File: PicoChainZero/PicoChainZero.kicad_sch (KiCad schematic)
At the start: 16 parts, among them J1 RJ45, J2 RJ45, J4 Screw Terminal, J5 Conn_02x20_Odd_Even, J6 Screw Terminal, J7 USB_C_Receptacle_USB2.0_14P, U1 LM78M05_TO252, U2 PCA9615DP, U3 FT232RL

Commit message: Added licences and PDF schematics
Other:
- title: (none) -> PicoChain Zero Reference Device Implementation
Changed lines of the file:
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@@
 	(generator_version "8.0")
 	(paper "A4")
+	(title_block
+		(title "PicoChain Zero Reference Device Implementation")
+		(date "2024-08-22")
+		(rev "v1.1")
+		(comment 2 "http://www.tapr.org/OHL")
+		(comment 3 "Licence: The TAPR Open Hardware License")
+		(comment 4 "Author: Jason Alexander")
+	)
 	(junction
 		(at 180.34 100.33)

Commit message: Regenerated gerbers
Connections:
- net +5V: now also U3.4 (VCCIO)
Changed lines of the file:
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@@
+	(wire
+		(pts
+			(xy 107.95 53.34) (xy 107.95 57.15)
+		)
+		(stroke
+			(width 0)
+			(type default)
+		)
+	)
 	(wire
 		(pts
@@
 					(unit 1)
 				)
+			)
+		)
+	)
+	(symbol
+		(lib_id "power:+5V")
+		(at 107.95 53.34 0)
+		(unit 1)
+		(exclude_from_sim no)
+		(in_bom yes)
+		(on_board yes)
+		(dnp no)
+		(property "Reference" "#PWR024"
+			(at 107.95 57.15 0)
+			(effects
+				(font
+					(size 1.27 1.27)
+				)
+				(hide yes)
+			)
+		)
+		(property "Value" "+5V"
+			(at 105.918 49.53 0)
+			(effects
+				(font
+					(size 1.27 1.27)
+				)
+				(justify left)
+			)
+		)
+		(property "Footprint" ""
+			(at 107.95 53.34 0)
+			(effects
+				(font
+					(size 1.27 1.27)
+				)
+				(hide yes)
+			)
+		)
+		(property "Datasheet" ""
+			(at 107.95 53.34 0)
+			(effects
+				(font
+					(size 1.27 1.27)
+				)
+				(hide yes)
+			)
+		)
+		(property "Description" "Power symbol creates a global label with name \"+5V\""
+			(at 107.95 53.34 0)
+			(effects
+				(font
+					(size 1.27 1.27)
+				)
+				(hide yes)
+			)
+		)
+		(pin "1"
+		)
+		(instances
+			(project "PicoChainZero"
+				(path "/bf05c66b-7ba7-46d1-8dac-29939cd00b00"
+					(reference "#PWR024")
+					(unit 1)
+				)

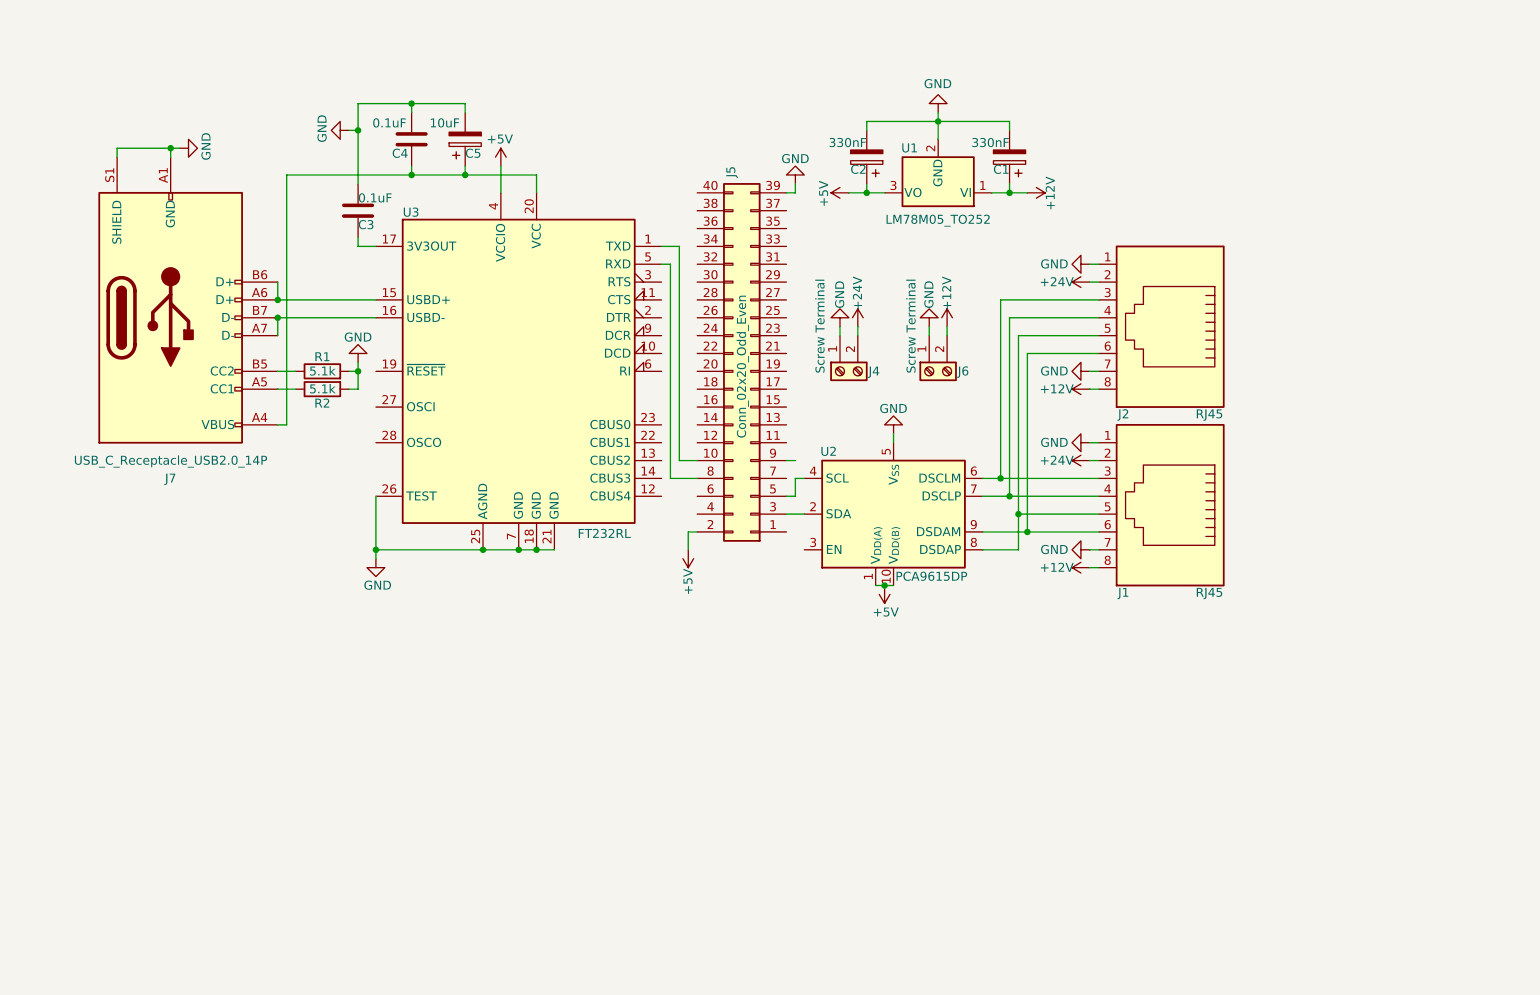
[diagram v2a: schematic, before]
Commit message: Updated PicoChainZero base board.
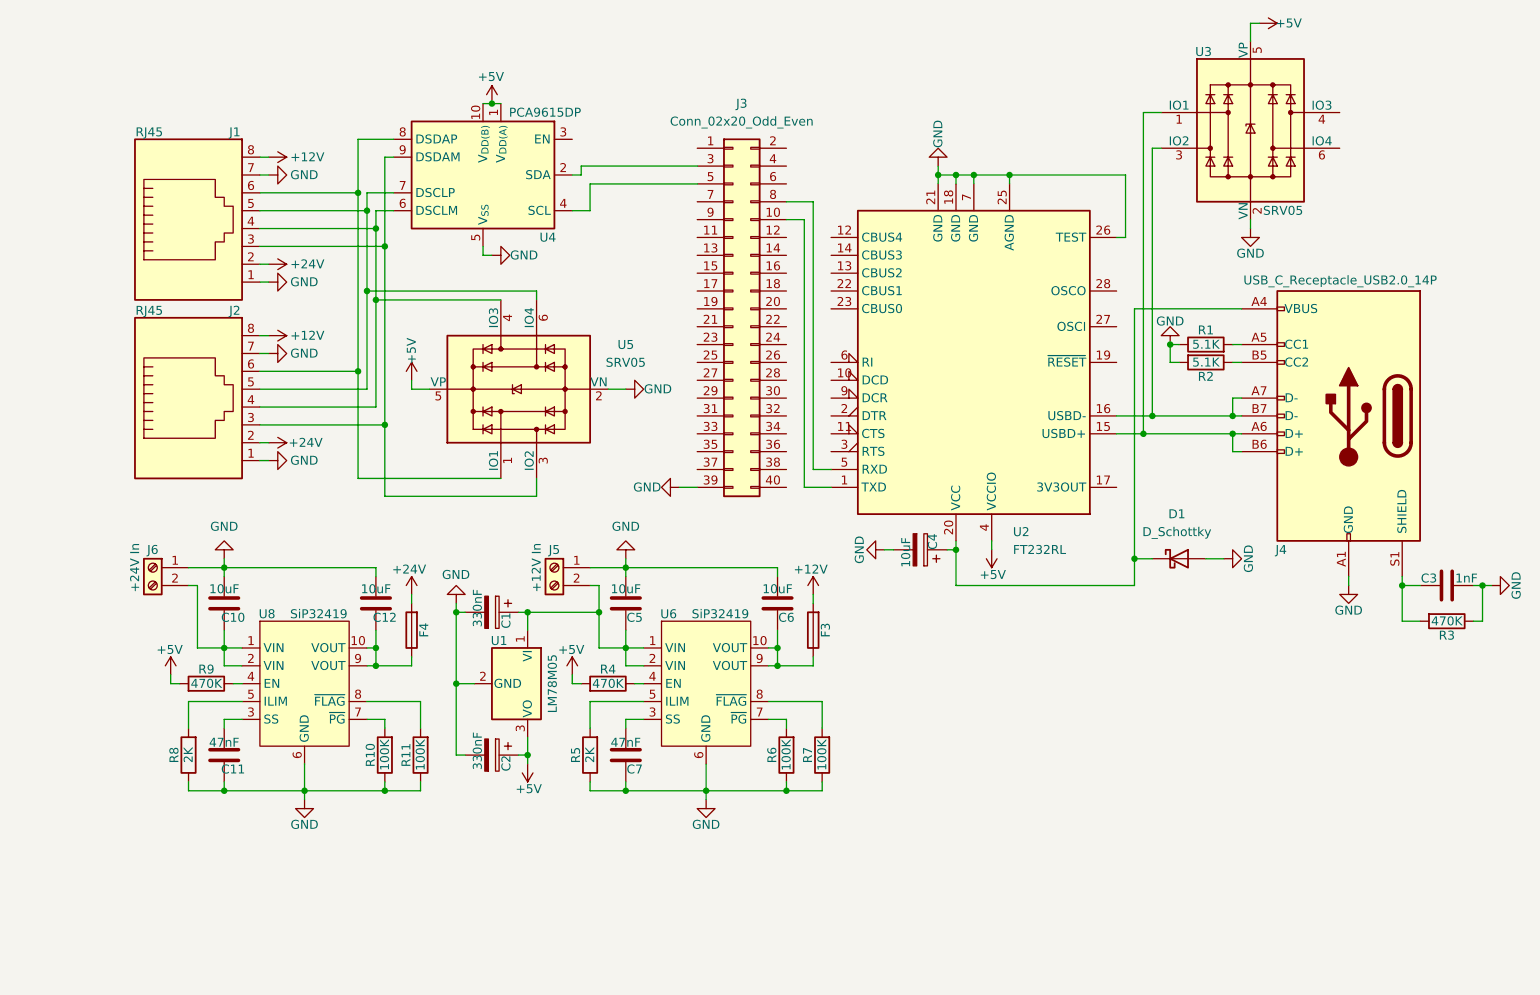
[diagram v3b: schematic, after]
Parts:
- removed C4: 0.1uF, Capacitor_SMD:C_0805_2012Metric, symbol Device:C
- removed C5: 10uF, Capacitor_Tantalum_SMD:CP_EIA-3216-18_Kemet-A, symbol Device:C_Polarized
- removed J4: Screw Terminal, TerminalBlock_Phoenix:TerminalBlock_Phoenix_MKDS-1,5-2-5.08_1x02_P5.08mm_Horizontal, symbol Connector:Screw_Terminal_01x02
- removed J5: Conn_02x20_Odd_Even, Connector_PinHeader_2.54mm:PinHeader_2x20_P2.54mm_Vertical, symbol Connector_Generic:Conn_02x20_Odd_Even
- removed J7: USB_C_Receptacle_USB2.0_14P, Connector_USB:USB_C_Receptacle_GCT_USB4085, symbol Connector:USB_C_Receptacle_USB2.0_14P
- removed U3: FT232RL, Package_SO:SSOP-28_5.3x10.2mm_P0.65mm, symbol Interface_USB:FT232RL
- added C10, C12, C5, C6: 10uF, Capacitor_SMD:C_0805_2012Metric, symbol Device:C
- added C11, C7: 47nF, Capacitor_SMD:C_0805_2012Metric, symbol Device:C
- added C4: 10uF, Capacitor_Tantalum_SMD:CP_EIA-3216-18_Kemet-A, symbol Device:C_Polarized
- added D1: D_Schottky, Diode_SMD:D_SMA, symbol Device:D_Schottky
- added F3, F4: Fuse, Fuse:Fuse_0805_2012Metric, symbol Device:Fuse
- added J3: Conn_02x20_Odd_Even, Connector_PinHeader_2.54mm:PinHeader_2x20_P2.54mm_Vertical, symbol Connector_Generic:Conn_02x20_Odd_Even
- added J4: USB_C_Receptacle_USB2.0_14P, Connector_USB:USB_C_Receptacle_GCT_USB4085, symbol Connector:USB_C_Receptacle_USB2.0_14P
- added J5: +12V In, TerminalBlock_Phoenix:TerminalBlock_Phoenix_MKDS-1,5-2-5.08_1x02_P5.08mm_Horizontal, symbol Connector:Screw_Terminal_01x02
- added R10, R11, R6, R7: 100K, Resistor_SMD:R_0805_2012Metric, symbol Device:R
- added R3, R4, R9: 470K, Resistor_SMD:R_0805_2012Metric, symbol Device:R
- added R5, R8: 2K, Resistor_SMD:R_0805_2012Metric, symbol Device:R
- added U2: FT232RL, Package_SO:SSOP-28_5.3x10.2mm_P0.65mm, symbol Interface_USB:FT232RL
- added U3, U5: SRV05, Package_TO_SOT_SMD:SOT-23-6, symbol Power_Protection:SRV05-4
- added U6, U8: SiP32419, Package_DFN_QFN:DFN-10-1EP_3x3mm_P0.5mm_EP1.65x2.38mm, symbol SiP32419:SiP32419
- C3: value 0.1uF -> 1nF; footprint Capacitor_SMD:C_0805_2012Metric -> Capacitor_SMD:C_1206_3216Metric
- J6: value Screw Terminal -> +24V In
- R1, R2: value 5.1k -> 5.1K
- U1: value LM78M05_TO252 -> LM78M05
- renumbered U2 to U4
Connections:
- net +12V: now also F3.2; no longer C1.1, J6.2 (Pin_2), U1.1 (VI)
- net +24V: now also F4.2
- net +5V: now also R4.2, R9.2, U2.4 (VCCIO), U3.5 (VP), U5.5 (VP)
- net GND: now also C3.2, R1.1, C10.1, C11.2, C12.1, C4.2, C5.1, C6.1, C7.2, D1.2 (A), J3.39 (Pin_39), J4.A1 (GND), J4.A12 (GND), J4.B1 (GND), J4.B12 (GND), J5.1 (Pin_1), R10.1, R11.1, R3.1, R5.1, R6.1, R7.1, R8.1, U2.18 (GND), U2.21 (GND), U2.25 (AGND), U2.26 (TEST), U2.7 (GND), U3.2 (VN), U5.2 (VN), U6.6 (GND), U8.6 (GND); no longer C3.1, R1.2
- net at R2.1: now also J4.B5 (CC2)
- net at U4.2 (SDA): now also J3.3 (Pin_3)
- net at U4.4 (SCL): now also J3.5 (Pin_5)
- net at J1.3, J2.3: now also U4.9 (DSDAM), U5.3 (IO2); no longer U4.6 (DSCLM)
- net at J1.4, J2.4: now also U4.6 (DSCLM), U5.4 (IO3); no longer U4.7 (DSCLP)
- net at J1.5, J2.5: now also U4.7 (DSCLP), U5.6 (IO4); no longer U4.8 (DSDAP)
- net at J1.6, J2.6: now also U4.8 (DSDAP), U5.1 (IO1); no longer U4.9 (DSDAM)
- new net: C1.1, C5.2, J5.2 (Pin_2), U1.1 (VI), U6.1 (VIN), U6.2 (VIN)
- new net: C6.2, F3.1, U6.10 (VOUT), U6.9 (VOUT)
- new net: C7.1, U6.3 (SS)
- new net: R4.1, U6.4 (EN)
- new net: R5.2, U6.5 (ILIM)
- new net: R6.2, U6.7 (~{PG})
- new net: R7.2, U6.8 (~{FLAG})
- new net: C3.1, J4.S1 (SHIELD), R3.2
- new net: C12.2, F4.1, U8.10 (VOUT), U8.9 (VOUT)
- new net: C10.2, J6.2 (Pin_2), U8.1 (VIN), U8.2 (VIN)
- new net: C4.1, D1.1 (K), J4.A4 (VBUS), J4.A9 (VBUS), J4.B4 (VBUS), J4.B9 (VBUS), U2.20 (VCC)
- new net: R8.2, U8.5 (ILIM)
- new net: J3.10 (Pin_10), U2.1 (TXD)
- new net: J4.A6 (D+), J4.B6 (D+), U2.15 (USBD+), U3.1 (IO1)
- new net: J4.A7 (D-), J4.B7 (D-), U2.16 (USBD-), U3.3 (IO2)
- new net: J3.8 (Pin_8), U2.5 (RXD)
- new net: R9.1, U8.4 (EN)
- new net: C11.1, U8.3 (SS)
- new net: J4.A5 (CC1), R1.2
- new net: R11.2, U8.8 (~{FLAG})
- new net: R10.2, U8.7 (~{PG})
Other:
- title: PicoChain Zero Reference Device Implementation -> PicoChain Generic Reference Device Implementation
- moved on the sheet: C1, C2, J1, J2, U1, U4

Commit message: Updated PicoChainZero PCB layout and generated Gerbers.
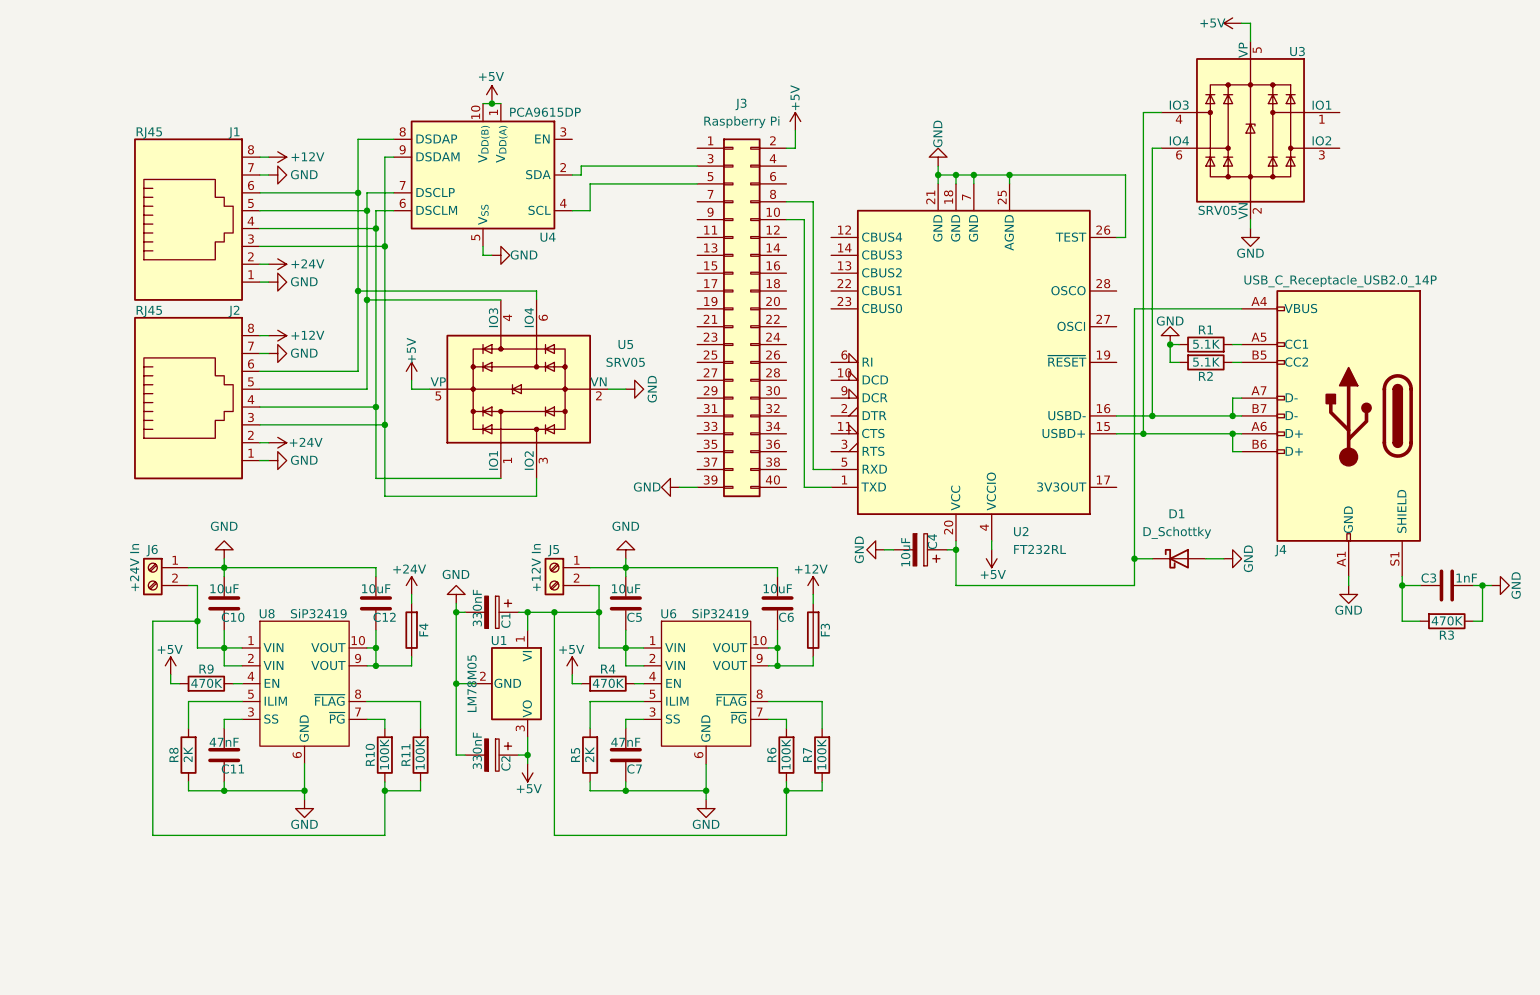
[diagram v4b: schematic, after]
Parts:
- J3: value Conn_02x20_Odd_Even -> Raspberry Pi
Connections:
- net +5V: now also J3.2 (Pin_2)
- net GND: no longer R10.1, R11.1, R6.1, R7.1
- net at J1.4, J2.4, U4.6 (DSCLM): now also U5.1 (IO1); no longer U5.4 (IO3)
- net at J1.5, J2.5, U4.7 (DSCLP): now also U5.4 (IO3); no longer U5.6 (IO4)
- net at J1.6, J2.6, U4.8 (DSDAP): now also U5.6 (IO4); no longer U5.1 (IO1)
- net at C1.1, C5.2, J5.2 (Pin_2)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: now also R6.1, R7.1
- net at C10.2, J6.2 (Pin_2), U8.1 (VIN)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: now also R10.1, R11.1
- net at J4.A6 (D+), J4.B6 (D+), U2.15 (USBD+): now also U3.4 (IO3); no longer U3.1 (IO1)
- net at J4.A7 (D-), J4.B7 (D-), U2.16 (USBD-): now also U3.6 (IO4); no longer U3.3 (IO2)

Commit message: Updated to 1.2
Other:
- moved on the sheet: C11, C7, R5, R8
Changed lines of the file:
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@@
 (kicad_sch
-	(version 20231120)
+	(version 20250114)
 	(generator "eeschema")
-	(generator_version "8.0")
+	(generator_version "9.0")
 	(paper "A4")
 	(title_block
 		(title "PicoChain Generic Reference Device Implementation")
 		(date "2024-08-22")
-		(rev "v1.1")
+		(rev "v1.2")
 		(comment 2 "http://www.tapr.org/OHL")
 		(comment 3 "Licence: The TAPR Open Hardware License")
@@
 	)
 	(junction
-		(at 125.73 142.24)
+		(at 127 142.24)
 		(diameter 0)
 		(color 0 0 0 0)
@@
 	)
 	(junction
-		(at 68.58 142.24)
+		(at 69.85 142.24)
 		(diameter 0)
 		(color 0 0 0 0)
@@
 	(wire
 		(pts
-			(xy 71.12 132.08) (xy 68.58 132.08)
+			(xy 71.12 132.08) (xy 69.85 132.08)
 		)
 		(stroke
@@
 	(wire
 		(pts
-			(xy 120.65 142.24) (xy 125.73 142.24)
+			(xy 121.92 142.24) (xy 127 142.24)
 		)
 		(stroke
@@
 	(wire
 		(pts
-			(xy 120.65 133.35) (xy 120.65 129.54)
+			(xy 121.92 133.35) (xy 121.92 129.54)
 		)
 		(stroke
@@
 	(wire
 		(pts
-			(xy 68.58 132.08) (xy 68.58 133.35)
+			(xy 69.85 132.08) (xy 69.85 133.35)
 		)
 		(stroke
@@
 	(wire
 		(pts
-			(xy 120.65 129.54) (xy 128.27 129.54)
+			(xy 121.92 129.54) (xy 128.27 129.54)
 		)
 		(stroke
@@
 	(wire
 		(pts
-			(xy 68.58 142.24) (xy 68.58 140.97)
+			(xy 69.85 142.24) (xy 69.85 140.97)
 		)
 		(stroke
@@
 	(wire
 		(pts
-			(xy 63.5 140.97) (xy 63.5 142.24)
+			(xy 64.77 140.97) (xy 64.77 142.24)
 		)
 		(stroke
@@
 	(wire
 		(pts
-			(xy 63.5 133.35) (xy 63.5 129.54)
+			(xy 64.77 133.35) (xy 64.77 129.54)
 		)
 		(stroke
@@
 	(wire
 		(pts
-			(xy 120.65 140.97) (xy 120.65 142.24)
+			(xy 121.92 140.97) (xy 121.92 142.24)
 		)
 		(stroke
@@
 	(wire
 		(pts
-			(xy 137.16 142.24) (xy 125.73 142.24)
+			(xy 137.16 142.24) (xy 127 142.24)
 		)
 		(stroke
@@
 	(wire
 		(pts
-			(xy 128.27 132.08) (xy 125.73 132.08)
+			(xy 128.27 132.08) (xy 127 132.08)
 		)
 		(stroke
@@
 	(wire
 		(pts
-			(xy 63.5 129.54) (xy 71.12 129.54)
+			(xy 64.77 129.54) (xy 71.12 129.54)
 		)
 		(stroke
@@
 	(wire
 		(pts
-			(xy 125.73 132.08) (xy 125.73 133.35)
+			(xy 127 132.08) (xy 127 133.35)
 		)
 		(stroke
@@
 	(wire
 		(pts
-			(xy 63.5 142.24) (xy 68.58 142.24)
+			(xy 64.77 142.24) (xy 69.85 142.24)
 		)
 		(stroke
@@
 	(wire
 		(pts
-			(xy 80.01 142.24) (xy 68.58 142.24)
+			(xy 80.01 142.24) (xy 69.85 142.24)
 		)
 		(stroke
@@
 	(wire
 		(pts
-			(xy 125.73 142.24) (xy 125.73 140.97)
+			(xy 127 142.24) (xy 127 140.97)
 		)
 		(stroke
@@
 	(symbol
 		(lib_id "Device:R")
-		(at 120.65 137.16 180)
+		(at 121.92 137.16 180)
 		(unit 1)
 		(exclude_from_sim no)
@@
 		(dnp no)
 		(property "Reference" "R5"
-			(at 118.618 137.16 90)
+			(at 119.888 137.16 90)
 			(effects
 				(font
@@
 		)
 		(property "Value" "2K"
-			(at 120.65 137.16 90)
+			(at 121.92 137.16 90)
 			(effects
 				(font
@@
 		)
 		(property "Footprint" "Resistor_SMD:R_0805_2012Metric"
-			(at 122.428 137.16 90)
+			(at 123.698 137.16 90)
 			(effects
 				(font
@@
 		)
 		(property "Datasheet" "~"
-			(at 120.65 137.16 0)
+			(at 121.92 137.16 0)
 			(effects
 				(font
@@
 		)
 		(property "Description" "Resistor"
-			(at 120.65 137.16 0)
+			(at 121.92 137.16 0)
 			(effects
 				(font
@@
 	(symbol
 		(lib_id "Device:R")
-		(at 63.5 137.16 180)
+		(at 64.77 137.16 180)
 		(unit 1)
 		(exclude_from_sim no)
@@
 		(dnp no)
 		(property "Reference" "R8"
-			(at 61.468 137.16 90)
+			(at 62.738 137.16 90)
 			(effects
 				(font
@@
 		)
 		(property "Value" "2K"
-			(at 63.5 137.16 90)
+			(at 64.77 137.16 90)
 			(effects
 				(font
@@
 		)
 		(property "Footprint" "Resistor_SMD:R_0805_2012Metric"
-			(at 65.278 137.16 90)
+			(at 66.548 137.16 90)
 			(effects
 				(font
@@
 		)
 		(property "Datasheet" "~"
-			(at 63.5 137.16 0)
+			(at 64.77 137.16 0)
 			(effects
 				(font
@@
 		)
 		(property "Description" "Resistor"
-			(at 63.5 137.16 0)
+			(at 64.77 137.16 0)
 			(effects
 				(font
@@
 	(symbol
 		(lib_id "Device:C")
-		(at 68.58 137.16 0)
+		(at 69.85 137.16 0)
 		(unit 1)
 		(exclude_from_sim no)
@@
 		)
 		(property "Value" "47nF"
-			(at 68.58 135.382 0)
+			(at 69.85 135.382 0)
 			(effects
 				(font
@@
 		)
 		(property "Footprint" "Capacitor_SMD:C_0805_2012Metric"
-			(at 69.5452 140.97 0)
+			(at 70.8152 140.97 0)
 			(effects
 				(font
@@
 		)
 		(property "Datasheet" "~"
-			(at 68.58 137.16 0)
+			(at 69.85 137.16 0)
 			(effects
 				(font
@@
 		)
 		(property "Description" "Unpolarized capacitor"
-			(at 68.58 137.16 0)
+			(at 69.85 137.16 0)
 			(effects
 				(font
@@
 	(symbol
 		(lib_id "Device:C")
-		(at 125.73 137.16 0)
+		(at 127 137.16 0)
 		(unit 1)
 		(exclude_from_sim no)
@@
 		(dnp no)
 		(property "Reference" "C7"
-			(at 127 139.192 0)
+			(at 128.27 139.192 0)
 			(effects
 				(font
@@
 		)
 		(property "Value" "47nF"
-			(at 125.73 135.382 0)
+			(at 127 135.382 0)
 			(effects
 				(font
@@
 		)
 		(property "Footprint" "Capacitor_SMD:C_0805_2012Metric"
-			(at 126.6952 140.97 0)
+			(at 127.9652 140.97 0)
 			(effects
 				(font
@@
 		)
 		(property "Datasheet" "~"
-			(at 125.73 137.16 0)
+			(at 127 137.16 0)
 			(effects
 				(font
@@
 		)
 		(property "Description" "Unpolarized capacitor"
-			(at 125.73 137.16 0)
+			(at 127 137.16 0)
 			(effects
 				(font
@@
 		)
 	)
+	(embedded_fonts no)
 )

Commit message: Added more fuses to reference implementation
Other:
- title: PicoChain Generic Reference Device Implementation -> PicoChain RPi Reference Device Implementation
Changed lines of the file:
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@@
 	(paper "A4")
 	(title_block
-		(title "PicoChain Generic Reference Device Implementation")
-		(date "2024-08-22")
+		(title "PicoChain RPi Reference Device Implementation")
+		(date "2025-04-21")
 		(rev "v1.2")
 		(comment 2 "http://www.tapr.org/OHL")
